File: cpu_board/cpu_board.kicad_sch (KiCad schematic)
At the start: 0 parts

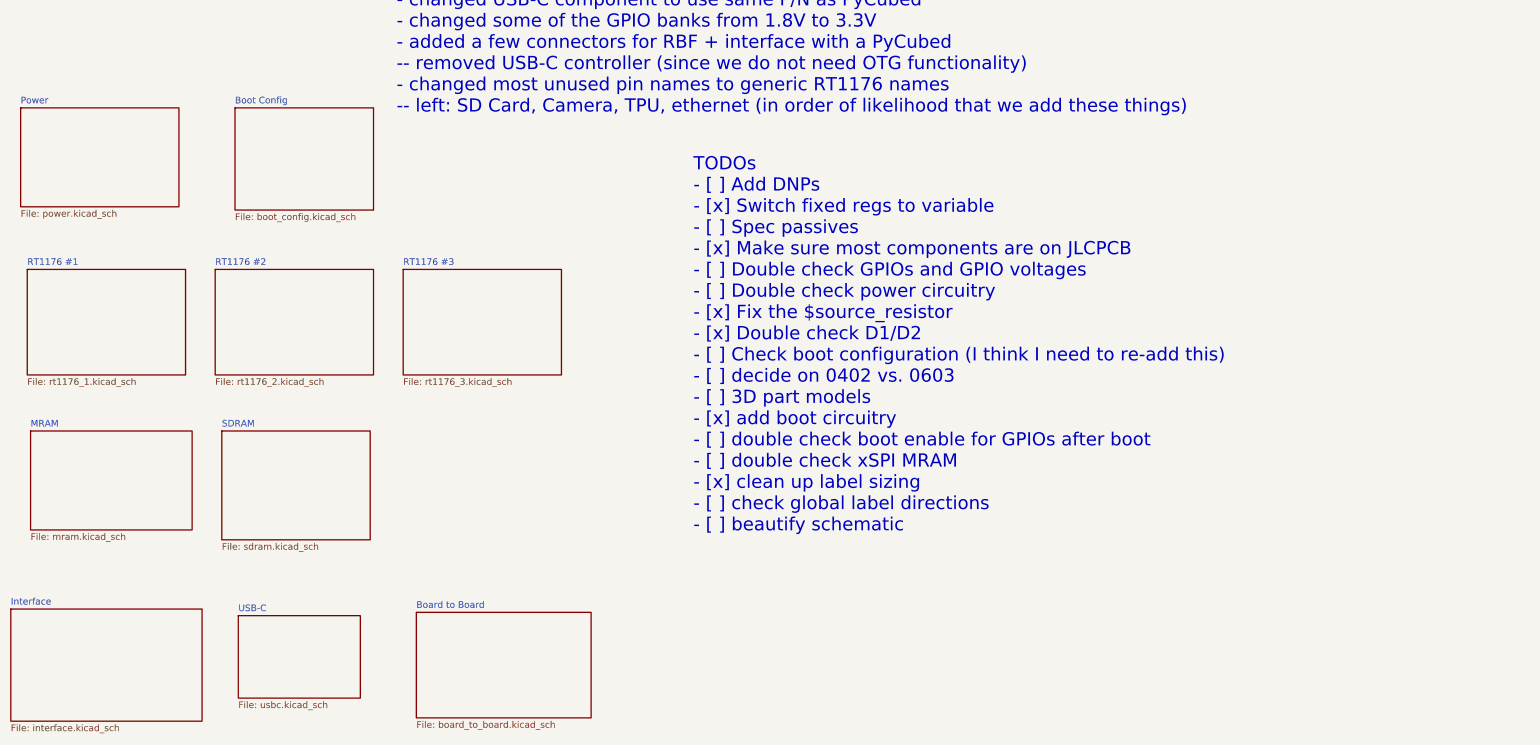
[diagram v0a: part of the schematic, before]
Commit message: clean up board2board connector and organize TODOs
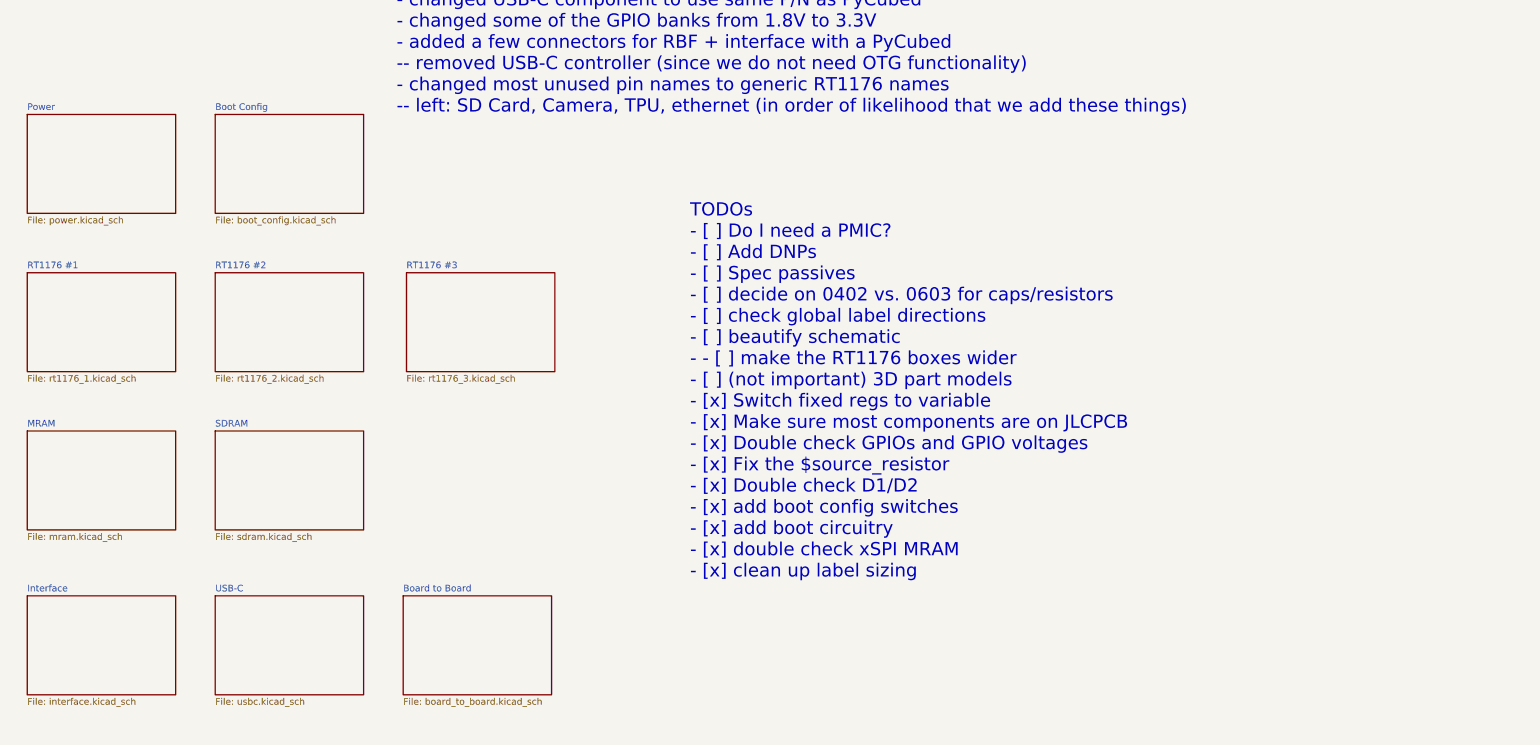
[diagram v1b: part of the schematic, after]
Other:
- note added: "TODOs - [ ] Do I need a PMIC? - [ ] Add DNPs - [ ] Spec passives - [ ] decide on 0402 vs. 0603 for caps/resistors - [ ] check global label directions - [ ] beautify schematic - - [ ] make the RT1176 boxes wider - [ ] (not important) 3D part models - [x] Switch fixed regs to variable - [x] Make sure most components are on JLCPCB - [x] Double check GPIOs and GPIO voltages - [x] Fix the $source_resi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"
- note removed: "TODOs - [ ] Add DNPs - [x] Switch fixed regs to variable - [ ] Spec passives - [x] Make sure most components are on JLCPCB - [ ] Double check GPIOs and GPIO voltages - [ ] Double check power circuitry - [x] Fix the $source_resistor - [x] Double check D1/D2 - [ ] Check boot configuration (I think I need to re-add this) - [ ] decide on 0402 vs. 0603 - [ ] 3D part models - [x] add boot circuitry - [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"
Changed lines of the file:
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@@
     (effects (font (size 2.54 2.54) (color 132 0 0 1)) (justify left bottom))
   )
-  (text "TODOs\n- [ ] Add DNPs\n- [x] Switch fixed regs to variable\n- [ ] Spec passives\n- [x] Make sure most components are on JLCPCB\n- [ ] Double check GPIOs and GPIO voltages\n- [ ] Double check power circuitry\n- [x] Fix the $source_resistor\n- [x] Double check D1/D2\n- [ ] Check boot configuration (I think I need to re-add this)\n- [ ] decide on 0402 vs. 0603\n- [ ] 3D part models\n- [x] add boot circuitry\n- [ ] double check boot enable for GPIOs after boot\n- [ ] double check xSPI MRAM\n- [x] clean up label sizing\n- [ ] check global label directions\n- [ ] beautify schematic"
-    (at 151.13 141.605 0)
+  (text "TODOs\n- [ ] Do I need a PMIC?\n- [ ] Add DNPs\n- [ ] Spec passives\n- [ ] decide on 0402 vs. 0603 for caps/resistors\n- [ ] check global label directions\n- [ ] beautify schematic\n- - [ ] make the RT1176 boxes wider\n- [ ] (not important) 3D part models\n- [x] Switch fixed regs to variable\n- [x] Make sure most components are on JLCPCB\n- [x] Double check GPIOs and GPIO voltages\n- [x] Fix the $source_resistor\n- [x] Double check D1/D2\n- [x] add boot config switches\n- [x] add boot circuitry\n- [x] double check xSPI MRAM\n- [x] clean up label sizing"
+    (at 150.495 150.495 0)
     (effects (font (size 2.54 2.54)) (justify left bottom))
   )
-  (sheet (at 95.25 90.805) (size 30.48 20.32) (fields_autoplaced)
+  (sheet (at 95.885 91.44) (size 28.575 19.05) (fields_autoplaced)
     (stroke (width 0.1524) (type solid))
     (fill (color 0 0 0 0.0000))
-    (property "Sheetname" "RT1176 #3" (at 95.25 90.0934 0)
+    (property "Sheetname" "RT1176 #3" (at 95.885 90.7284 0)
       (effects (font (size 1.27 1.27)) (justify left bottom))
     )
-    (property "Sheetfile" "rt1176_3.kicad_sch" (at 95.25 111.7096 0)
+    (property "Sheetfile" "rt1176_3.kicad_sch" (at 95.885 111.0746 0)
       (effects (font (size 1.27 1.27)) (justify left top))
     )
@@
     )
   )
-  (sheet (at 59.055 90.805) (size 30.48 20.32) (fields_autoplaced)
+  (sheet (at 59.055 91.44) (size 28.575 19.05) (fields_autoplaced)
     (stroke (width 0.1524) (type solid))
     (fill (color 0 0 0 0.0000))
-    (property "Sheetname" "RT1176 #2" (at 59.055 90.0934 0)
+    (property "Sheetname" "RT1176 #2" (at 59.055 90.7284 0)
       (effects (font (size 1.27 1.27)) (justify left bottom))
     )
-    (property "Sheetfile" "rt1176_2.kicad_sch" (at 59.055 111.7096 0)
+    (property "Sheetfile" "rt1176_2.kicad_sch" (at 59.055 111.0746 0)
       (effects (font (size 1.27 1.27)) (justify left top))
     )
@@
     )
   )
-  (sheet (at 60.325 121.92) (size 28.575 20.955) (fields_autoplaced)
+  (sheet (at 59.055 121.92) (size 28.575 19.05) (fields_autoplaced)
     (stroke (width 0.1524) (type solid))
     (fill (color 0 0 0 0.0000))
-    (property "Sheetname" "SDRAM" (at 60.325 121.2084 0)
+    (property "Sheetname" "SDRAM" (at 59.055 121.2084 0)
       (effects (font (size 1.27 1.27)) (justify left bottom))
     )
-    (property "Sheetfile" "sdram.kicad_sch" (at 60.325 143.4596 0)
+    (property "Sheetfile" "sdram.kicad_sch" (at 59.055 141.5546 0)
       (effects (font (size 1.27 1.27)) (justify left top))
     )
@@
     )
   )
-  (sheet (at 21.59 59.69) (size 30.48 19.05) (fields_autoplaced)
+  (sheet (at 22.86 60.96) (size 28.575 19.05) (fields_autoplaced)
     (stroke (width 0.1524) (type solid))
     (fill (color 0 0 0 0.0000))
-    (property "Sheetname" "Power" (at 21.59 58.9784 0)
+    (property "Sheetname" "Power" (at 22.86 60.2484 0)
       (effects (font (size 1.27 1.27)) (justify left bottom))
     )
-    (property "Sheetfile" "power.kicad_sch" (at 21.59 79.3246 0)
+    (property "Sheetfile" "power.kicad_sch" (at 22.86 80.5946 0)
       (effects (font (size 1.27 1.27)) (justify left top))
     )
@@
     )
   )
-  (sheet (at 62.865 59.69) (size 26.67 19.685) (fields_autoplaced)
+  (sheet (at 59.055 60.96) (size 28.575 19.05) (fields_autoplaced)
     (stroke (width 0.1524) (type solid))
     (fill (color 0 0 0 0.0000))
-    (property "Sheetname" "Boot Config" (at 62.865 58.9784 0)
+    (property "Sheetname" "Boot Config" (at 59.055 60.2484 0)
       (effects (font (size 1.27 1.27)) (justify left bottom))
     )
-    (property "Sheetfile" "boot_config.kicad_sch" (at 62.865 79.9596 0)
+    (property "Sheetfile" "boot_config.kicad_sch" (at 59.055 80.5946 0)
       (effects (font (size 1.27 1.27)) (justify left top))
     )
@@
     )
   )
-  (sheet (at 23.495 121.92) (size 31.115 19.05) (fields_autoplaced)
+  (sheet (at 22.86 121.92) (size 28.575 19.05) (fields_autoplaced)
     (stroke (width 0.1524) (type solid))
     (fill (color 0 0 0 0.0000))
-    (property "Sheetname" "MRAM" (at 23.495 121.2084 0)
+    (property "Sheetname" "MRAM" (at 22.86 121.2084 0)
       (effects (font (size 1.27 1.27)) (justify left bottom))
     )
-    (property "Sheetfile" "mram.kicad_sch" (at 23.495 141.5546 0)
+    (property "Sheetfile" "mram.kicad_sch" (at 22.86 141.5546 0)
       (effects (font (size 1.27 1.27)) (justify left top))
     )
@@
     )
   )
-  (sheet (at 22.86 90.805) (size 30.48 20.32) (fields_autoplaced)
+  (sheet (at 22.86 91.44) (size 28.575 19.05) (fields_autoplaced)
     (stroke (width 0.1524) (type solid))
     (fill (color 0 0 0 0.0000))
-    (property "Sheetname" "RT1176 #1" (at 22.86 90.0934 0)
+    (property "Sheetname" "RT1176 #1" (at 22.86 90.7284 0)
       (effects (font (size 1.27 1.27)) (justify left bottom))
     )
-    (property "Sheetfile" "rt1176_1.kicad_sch" (at 22.86 111.7096 0)
+    (property "Sheetfile" "rt1176_1.kicad_sch" (at 22.86 111.0746 0)
       (effects (font (size 1.27 1.27)) (justify left top))
     )
@@
     )
   )
-  (sheet (at 19.685 156.21) (size 36.83 21.59) (fields_autoplaced)
+  (sheet (at 22.86 153.67) (size 28.575 19.05) (fields_autoplaced)
     (stroke (width 0.1524) (type solid))
     (fill (color 0 0 0 0.0000))
-    (property "Sheetname" "Interface" (at 19.685 155.4984 0)
+    (property "Sheetname" "Interface" (at 22.86 152.9584 0)
       (effects (font (size 1.27 1.27)) (justify left bottom))
     )
-    (property "Sheetfile" "interface.kicad_sch" (at 19.685 178.3846 0)
+    (property "Sheetfile" "interface.kicad_sch" (at 22.86 173.3046 0)
       (effects (font (size 1.27 1.27)) (justify left top))
     )
@@
     )
   )
-  (sheet (at 63.5 157.48) (size 23.495 15.875) (fields_autoplaced)
+  (sheet (at 59.055 153.67) (size 28.575 19.05) (fields_autoplaced)
     (stroke (width 0.1524) (type solid))
     (fill (color 0 0 0 0.0000))
-    (property "Sheetname" "USB-C" (at 63.5 156.7684 0)
+    (property "Sheetname" "USB-C" (at 59.055 152.9584 0)
       (effects (font (size 1.27 1.27)) (justify left bottom))
     )
-    (property "Sheetfile" "usbc.kicad_sch" (at 63.5 173.9396 0)
+    (property "Sheetfile" "usbc.kicad_sch" (at 59.055 173.3046 0)
       (effects (font (size 1.27 1.27)) (justify left top))
     )
@@
     )
   )
-  (sheet (at 97.79 156.845) (size 33.655 20.32) (fields_autoplaced)
+  (sheet (at 95.25 153.67) (size 28.575 19.05) (fields_autoplaced)
     (stroke (width 0.1524) (type solid))
     (fill (color 0 0 0 0.0000))
-    (property "Sheetname" "Board to Board" (at 97.79 156.1334 0)
+    (property "Sheetname" "Board to Board" (at 95.25 152.9584 0)
       (effects (font (size 1.27 1.27)) (justify left bottom))
     )
-    (property "Sheetfile" "board_to_board.kicad_sch" (at 97.79 177.7496 0)
+    (property "Sheetfile" "board_to_board.kicad_sch" (at 95.25 173.3046 0)
       (effects (font (size 1.27 1.27)) (justify left top))
     )

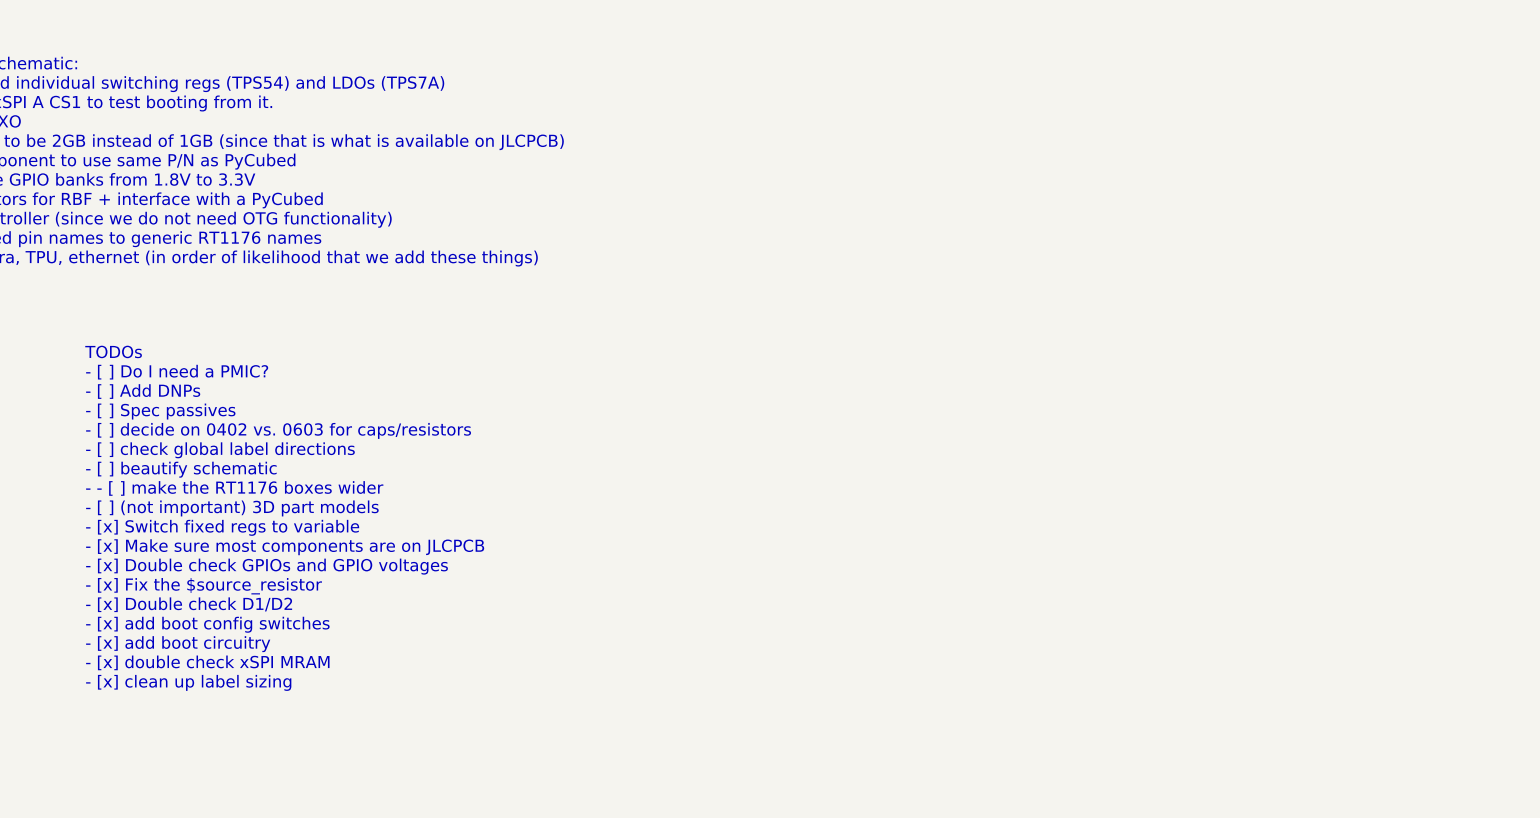
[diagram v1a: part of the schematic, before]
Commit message: clean up silkscreen
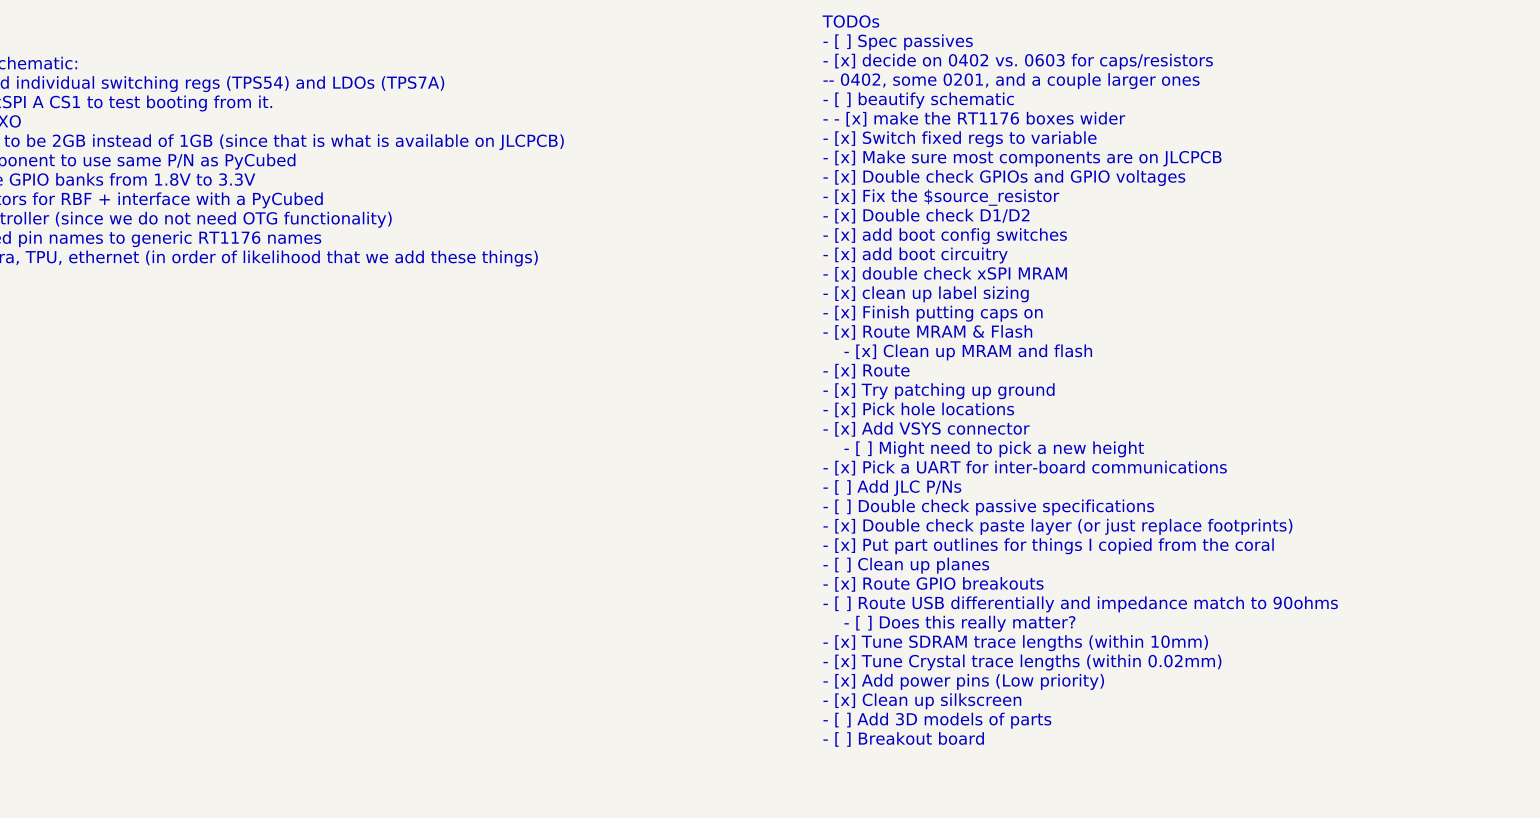
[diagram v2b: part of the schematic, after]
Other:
- note added: "TODOs - [ ] Spec passives - [x] decide on 0402 vs. 0603 for caps/resistors -- 0402, some 0201, and a couple larger ones - [ ] beautify schematic - - [x] make the RT1176 boxes wider - [x] Switch fixed regs to variable - [x] Make sure most components are on JLCPCB - [x] Double check GPIOs and GPIO voltages - [x] Fix the $source_resistor - [x] Double check D1/D2 - [x] add boot config switches - [x] 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"
- note removed: "TODOs - [ ] Do I need a PMIC? - [ ] Add DNPs - [ ] Spec passives - [ ] decide on 0402 vs. 0603 for caps/resistors - [ ] check global label directions - [ ] beautify schematic - - [ ] make the RT1176 boxes wider - [ ] (not important) 3D part models - [x] Switch fixed regs to variable - [x] Make sure most components are on JLCPCB - [x] Double check GPIOs and GPIO voltages - [x] Fix the $source_resi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"
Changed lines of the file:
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@@
     (effects (font (size 2.54 2.54) (color 132 0 0 1)) (justify left bottom))
   )
-  (text "TODOs\n- [ ] Do I need a PMIC?\n- [ ] Add DNPs\n- [ ] Spec passives\n- [ ] decide on 0402 vs. 0603 for caps/resistors\n- [ ] check global label directions\n- [ ] beautify schematic\n- - [ ] make the RT1176 boxes wider\n- [ ] (not important) 3D part models\n- [x] Switch fixed regs to variable\n- [x] Make sure most components are on JLCPCB\n- [x] Double check GPIOs and GPIO voltages\n- [x] Fix the $source_resistor\n- [x] Double check D1/D2\n- [x] add boot config switches\n- [x] add boot circuitry\n- [x] double check xSPI MRAM\n- [x] clean up label sizing"
-    (at 150.495 150.495 0)
+  (text "TODOs\n- [ ] Spec passives\n- [x] decide on 0402 vs. 0603 for caps/resistors\n-- 0402, some 0201, and a couple larger ones\n- [ ] beautify schematic\n- - [x] make the RT1176 boxes wider\n- [x] Switch fixed regs to variable\n- [x] Make sure most components are on JLCPCB\n- [x] Double check GPIOs and GPIO voltages\n- [x] Fix the $source_resistor\n- [x] Double check D1/D2\n- [x] add boot config switches\n- [x] add boot circuitry\n- [x] double check xSPI MRAM\n- [x] clean up label sizing\n- [x] Finish putting caps on\n- [x] Route MRAM & Flash\n    - [x] Clean up MRAM and flash\n- [x] Route \n- [x] Try patching up ground\n- [x] Pick hole locations\n- [x] Add VSYS connector\n    - [ ] Might need to pick a new height\n- [x] Pick a UART for inter-board communications\n- [ ] Add JLC P/Ns\n- [ ] Double check passive specifications\n- [x] Double check paste layer (or just replace footprints)\n- [x] Put part outlines for things I copied from the coral\n- [ ] Clean up planes\n- [x] Route GPIO breakouts\n- [ ] Route USB differentially and impedance match to 90ohms\n    - [ ] Does this really matter?\n- [x] Tune SDRAM trace lengths (within 10mm)\n- [x] Tune Crystal trace lengths (within 0.02mm)\n- [x] Add power pins (Low priority)\n- [x] Clean up silkscreen\n- [ ] Add 3D models of parts\n- [ ] Breakout board"
+    (at 306.07 162.56 0)
     (effects (font (size 2.54 2.54)) (justify left bottom))
   )
